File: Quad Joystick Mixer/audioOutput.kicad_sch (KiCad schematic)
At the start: 26 parts, among them J2 NMJ6HCD, U4 OPA1692xD

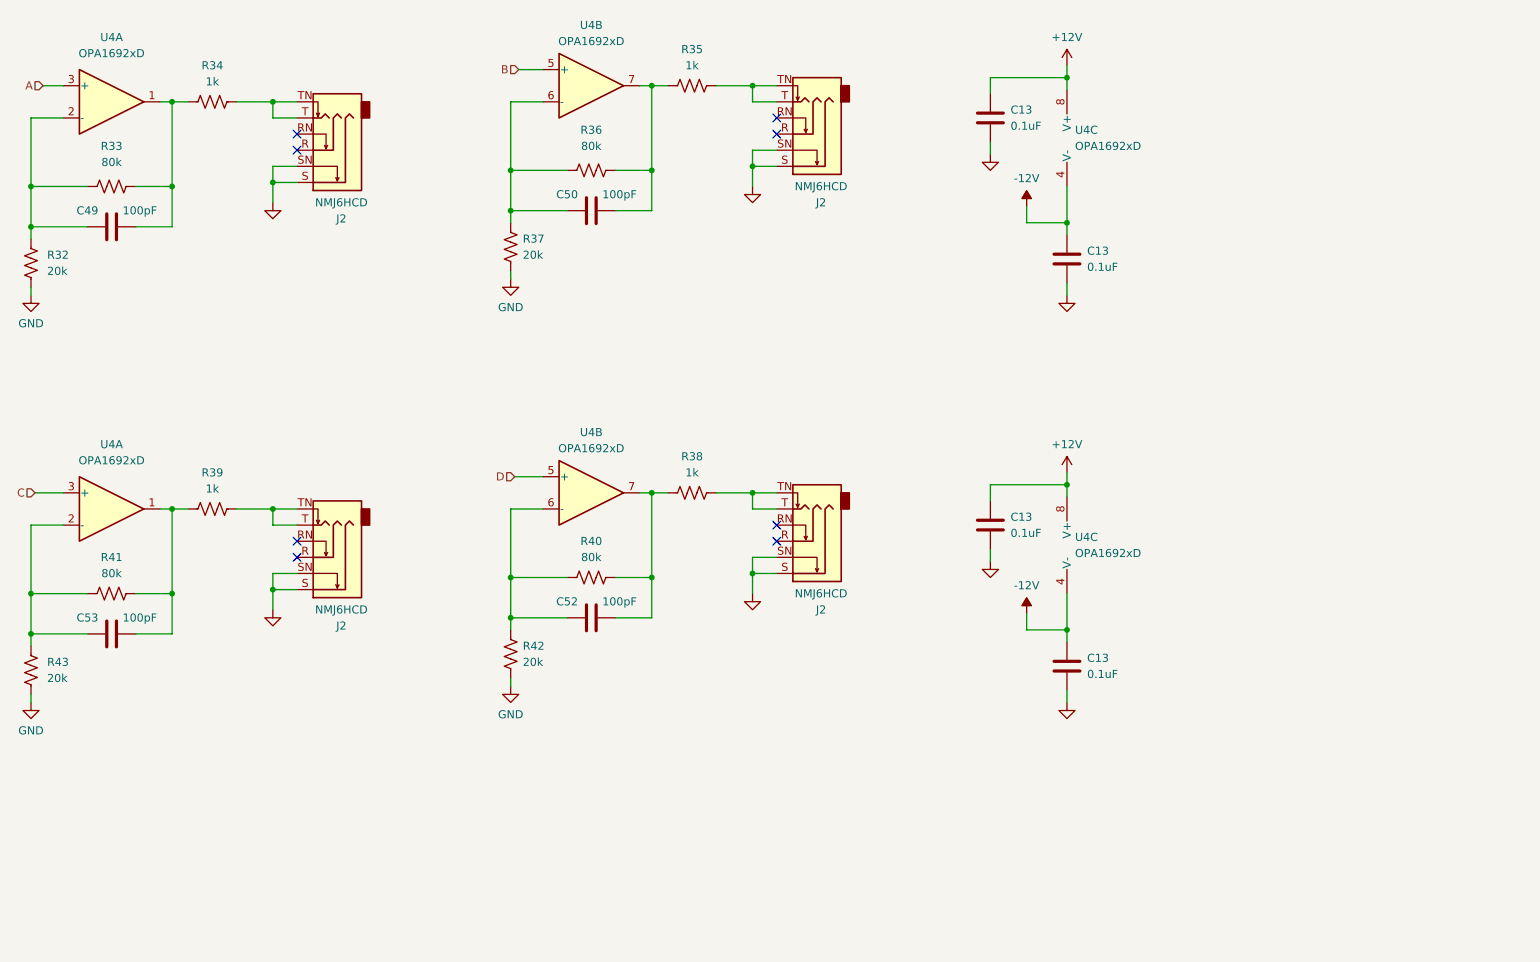
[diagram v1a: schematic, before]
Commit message: add in rotary circuit and some docs
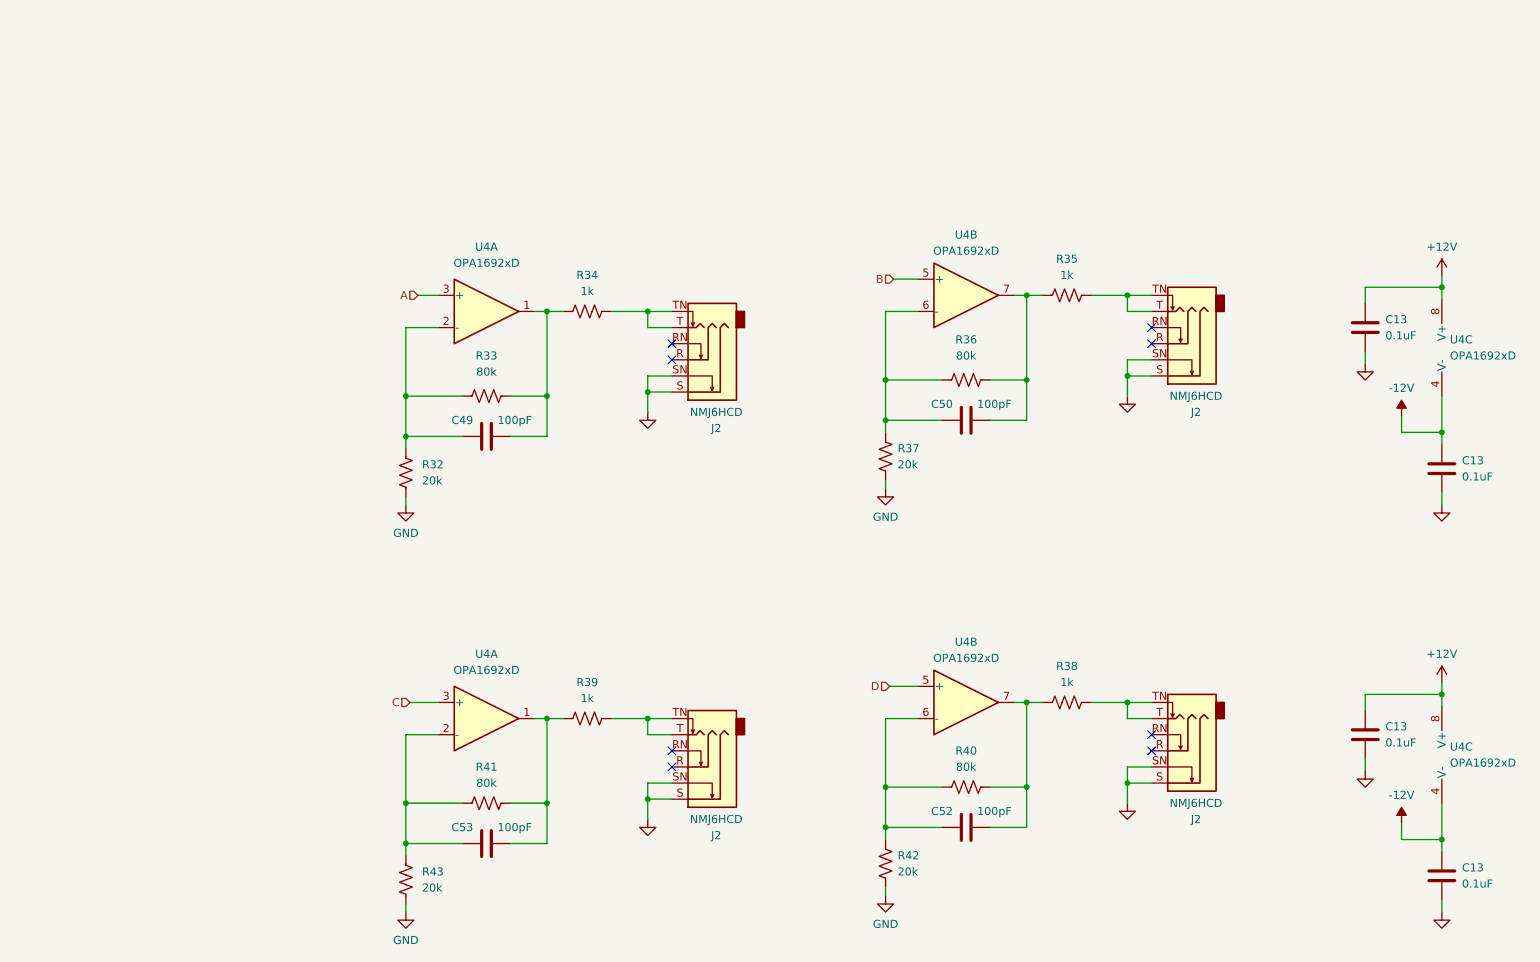
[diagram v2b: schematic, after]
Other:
- moved on the sheet: C13, C49, C50, C52, C53, J2, R32, R33, R34, R35, R36, R37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

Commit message: finished first draft of the schematic
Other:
- note added: "Audio Outputs"
- title: (none) -> Quadrophonic Joystick Mixer
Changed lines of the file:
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@@
   (paper "B")
   (title_block
+    (title "Quadrophonic Joystick Mixer")
     (date "2024-02-14")
+    (rev "P1")
   )
   (junction (at 224.155 147.32) (diameter 0) (color 0 0 0 0)
@@
     (stroke (width 0) (type default))
   )
+  (text "Audio Outputs" (at 157.48 45.085 0)
+    (effects (font (size 3.81 3.81) (thickness 0.508) bold) (justify left bottom))
+  )
   (hierarchical_label "D" (shape input) (at 202.565 144.78 180) (fields_autoplaced)

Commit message: ok the draft wasn't done but now i think it is
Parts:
- added TP1 (x4): TestPoint, TestPoint:TestPoint_THTPad_D1.5mm_Drill0.7mm, symbol Connector:TestPoint
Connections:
- net at J2.T, J2.TN, R39.1: now also TP1.1
- net at J2.T, J2.TN, R38.1: now also TP1.1
- net at J2.T, J2.TN, R34.1: now also TP1.1
- net at J2.T, J2.TN, R35.1: now also TP1.1
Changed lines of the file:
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@@
     (rev "P1")
   )
+  (junction (at 161.29 149.86) (diameter 0) (color 0 0 0 0)
+  )
+  (junction (at 161.29 85.725) (diameter 0) (color 0 0 0 0)
+  )
   (junction (at 224.155 147.32) (diameter 0) (color 0 0 0 0)
   )
@@
   (junction (at 201.93 160.655) (diameter 0) (color 0 0 0 0)
   )
+  (junction (at 236.855 147.32) (diameter 0) (color 0 0 0 0)
+  )
   (junction (at 240.03 95.885) (diameter 0) (color 0 0 0 0)
   )
@@
   )
   (junction (at 240.03 147.32) (diameter 0) (color 0 0 0 0)
+  )
+  (junction (at 236.855 83.185) (diameter 0) (color 0 0 0 0)
   )
   (junction (at 164.465 149.86) (diameter 0) (color 0 0 0 0)
@@
     (stroke (width 0) (type default))
   )
+  (wire (pts (xy 236.855 77.47) (xy 236.855 83.185))
+    (stroke (width 0) (type default))
+  )
   (wire (pts (xy 148.59 105.41) (xy 142.875 105.41))
     (stroke (width 0) (type default))
   )
+  (wire (pts (xy 236.855 83.185) (xy 240.03 83.185))
+    (stroke (width 0) (type default))
+  )
   (wire (pts (xy 243.84 149.86) (xy 240.03 149.86))
     (stroke (width 0) (type default))
@@
     (stroke (width 0) (type default))
   )
-  (wire (pts (xy 158.75 85.725) (xy 164.465 85.725))
+  (wire (pts (xy 158.75 85.725) (xy 161.29 85.725))
+    (stroke (width 0) (type default))
+  )
+  (wire (pts (xy 161.29 80.645) (xy 161.29 85.725))
     (stroke (width 0) (type default))
   )
@@
     (stroke (width 0) (type default))
   )
+  (wire (pts (xy 161.29 144.145) (xy 161.29 149.86))
+    (stroke (width 0) (type default))
+  )
   (wire (pts (xy 126.365 179.07) (xy 126.365 180.34))
     (stroke (width 0) (type default))
@@
     (stroke (width 0) (type default))
   )
+  (wire (pts (xy 236.855 147.32) (xy 240.03 147.32))
+    (stroke (width 0) (type default))
+  )
   (wire (pts (xy 146.685 85.725) (xy 148.59 85.725))
     (stroke (width 0) (type default))
@@
     (stroke (width 0) (type default))
   )
-  (wire (pts (xy 234.315 147.32) (xy 240.03 147.32))
+  (wire (pts (xy 234.315 147.32) (xy 236.855 147.32))
     (stroke (width 0) (type default))
   )
@@
     (stroke (width 0) (type default))
   )
-  (wire (pts (xy 158.75 149.86) (xy 164.465 149.86))
+  (wire (pts (xy 158.75 149.86) (xy 161.29 149.86))
     (stroke (width 0) (type default))
   )
@@
     (stroke (width 0) (type default))
   )
+  (wire (pts (xy 240.03 142.24) (xy 236.855 142.24))
+    (stroke (width 0) (type default))
+  )
   (wire (pts (xy 168.275 152.4) (xy 164.465 152.4))
     (stroke (width 0) (type default))
@@
     (stroke (width 0) (type default))
   )
+  (wire (pts (xy 238.76 77.47) (xy 236.855 77.47))
+    (stroke (width 0) (type default))
+  )
   (wire (pts (xy 207.01 85.725) (xy 201.93 85.725))
     (stroke (width 0) (type default))
   )
+  (wire (pts (xy 163.83 144.145) (xy 161.29 144.145))
+    (stroke (width 0) (type default))
+  )
   (wire (pts (xy 224.155 167.005) (xy 224.155 160.655))
     (stroke (width 0) (type default))
@@
     (stroke (width 0) (type default))
   )
-  (wire (pts (xy 234.315 83.185) (xy 240.03 83.185))
+  (wire (pts (xy 234.315 83.185) (xy 236.855 83.185))
     (stroke (width 0) (type default))
   )
@@
     (stroke (width 0) (type default))
   )
+  (wire (pts (xy 162.56 80.645) (xy 161.29 80.645))
+    (stroke (width 0) (type default))
+  )
   (wire (pts (xy 146.685 149.86) (xy 148.59 149.86))
     (stroke (width 0) (type default))
@@
     (stroke (width 0) (type default))
   )
+  (wire (pts (xy 161.29 149.86) (xy 164.465 149.86))
+    (stroke (width 0) (type default))
+  )
   (wire (pts (xy 127 147.32) (xy 131.445 147.32))
     (stroke (width 0) (type default))
@@
     (stroke (width 0) (type default))
   )
+  (wire (pts (xy 236.855 142.24) (xy 236.855 147.32))
+    (stroke (width 0) (type default))
+  )
   (wire (pts (xy 243.84 93.345) (xy 240.03 93.345))
     (stroke (width 0) (type default))
   )
   (wire (pts (xy 222.25 83.185) (xy 224.155 83.185))
+    (stroke (width 0) (type default))
+  )
+  (wire (pts (xy 161.29 85.725) (xy 164.465 85.725))
     (stroke (width 0) (type default))
   )
@@
     )
   )
+  (symbol (lib_id "Connector:TestPoint") (at 240.03 142.24 270) (unit 1)
+    (in_bom yes) (on_board yes) (dnp no) (fields_autoplaced)
+    (property "Reference" "TP1" (at 245.745 142.24 90)
+      (effects (font (size 1.27 1.27)) (justify left))
+    )
+    (property "Value" "TestPoint" (at 242.062 144.145 0)
+      (effects (font (size 1.27 1.27)) (justify left) hide)
+    )
+    (property "Footprint" "TestPoint:TestPoint_THTPad_D1.5mm_Drill0.7mm" (at 240.03 147.32 0)
+      (effects (font (size 1.27 1.27)) hide)
+    )
+    (property "Datasheet" "~" (at 240.03 147.32 0)
+      (effects (font (size 1.27 1.27)) hide)
+    )
+    (pin "1")
+    (instances
+      (project "Quad Joystick Mixer"
+        (path "/e9da4955-68c1-4335-ab8e-8a9cc0328d2d/70e873e8-c2f7-42de-91d7-3f147d0d972e"
+          (reference "TP1") (unit 1)
+        )
+        (path "/e9da4955-68c1-4335-ab8e-8a9cc0328d2d/df381643-9329-42d2-97be-3d7265bc1cca"
+          (reference "TP19") (unit 1)
+        )
+      )
+    )
+  )
   (symbol (lib_id "power:GND") (at 126.365 180.34 0) (unit 1)
     (in_bom yes) (on_board yes) (dnp no) (fields_autoplaced)
@@
         (path "/e9da4955-68c1-4335-ab8e-8a9cc0328d2d/df381643-9329-42d2-97be-3d7265bc1cca"
           (reference "C54") (unit 1)
+        )
+      )
+    )
+  )
+  (symbol (lib_id "Connector:TestPoint") (at 162.56 80.645 270) (unit 1)
+    (in_bom yes) (on_board yes) (dnp no) (fields_autoplaced)
+    (property "Reference" "TP1" (at 168.275 80.645 90)
+      (effects (font (size 1.27 1.27)) (justify left))
+    )
+    (property "Value" "TestPoint" (at 164.592 82.55 0)
+      (effects (font (size 1.27 1.27)) (justify left) hide)
+    )
+    (property "Footprint" "TestPoint:TestPoint_THTPad_D1.5mm_Drill0.7mm" (at 162.56 85.725 0)
+      (effects (font (size 1.27 1.27)) hide)
+    )
+    (property "Datasheet" "~" (at 162.56 85.725 0)
+      (effects (font (size 1.27 1.27)) hide)
+    )
+    (pin "1")
+    (instances
+      (project "Quad Joystick Mixer"
+        (path "/e9da4955-68c1-4335-ab8e-8a9cc0328d2d/70e873e8-c2f7-42de-91d7-3f147d0d972e"
+          (reference "TP1") (unit 1)
+        )
+        (path "/e9da4955-68c1-4335-ab8e-8a9cc0328d2d/df381643-9329-42d2-97be-3d7265bc1cca"
+          (reference "TP16") (unit 1)
         )
       )
@@
     )
   )
+  (symbol (lib_id "Connector:TestPoint") (at 238.76 77.47 270) (unit 1)
+    (in_bom yes) (on_board yes) (dnp no) (fields_autoplaced)
+    (property "Reference" "TP1" (at 244.475 77.47 90)
+      (effects (font (size 1.27 1.27)) (justify left))
+    )
+    (property "Value" "TestPoint" (at 240.792 79.375 0)
+      (effects (font (size 1.27 1.27)) (justify left) hide)
+    )
+    (property "Footprint" "TestPoint:TestPoint_THTPad_D1.5mm_Drill0.7mm" (at 238.76 82.55 0)
+      (effects (font (size 1.27 1.27)) hide)
+    )
+    (property "Datasheet" "~" (at 238.76 82.55 0)
+      (effects (font (size 1.27 1.27)) hide)
+    )
+    (pin "1")
+    (instances
+      (project "Quad Joystick Mixer"
+        (path "/e9da4955-68c1-4335-ab8e-8a9cc0328d2d/70e873e8-c2f7-42de-91d7-3f147d0d972e"
+          (reference "TP1") (unit 1)
+        )
+        (path "/e9da4955-68c1-4335-ab8e-8a9cc0328d2d/df381643-9329-42d2-97be-3d7265bc1cca"
+          (reference "TP17") (unit 1)
+        )
+      )
+    )
+  )
   (symbol (lib_id "power:+12V") (at 289.56 80.01 0) (unit 1)
     (in_bom yes) (on_board yes) (dnp no) (fields_autoplaced)
@@
         )
       )
+    )
+  )
+  (symbol (lib_id "Connector:TestPoint") (at 163.83 144.145 270) (unit 1)
+    (in_bom yes) (on_board yes) (dnp no) (fields_autoplaced)
+    (property "Reference" "TP1" (at 169.545 144.145 90)
+      (effects (font (size 1.27 1.27)) (justify left))
+    )
+    (property "Value" "TestPoint" (at 165.862 146.05 0)
+      (effects (font (size 1.27 1.27)) (justify left) hide)
+    )
+    (property "Footprint" "TestPoint:TestPoint_THTPad_D1.5mm_Drill0.7mm" (at 163.83 149.225 0)
+      (effects (font (size 1.27 1.27)) hide)
+    )
+    (property "Datasheet" "~" (at 163.83 149.225 0)
+      (effects (font (size 1.27 1.27)) hide)
+    )
+    (pin "1")
+    (instances
+      (project "Quad Joystick Mixer"
+        (path "/e9da4955-68c1-4335-ab8e-8a9cc0328d2d/70e873e8-c2f7-42de-91d7-3f147d0d972e"
+          (reference "TP1") (unit 1)
+        )
+        (path "/e9da4955-68c1-4335-ab8e-8a9cc0328d2d/df381643-9329-42d2-97be-3d7265bc1cca"
+          (reference "TP18") (unit 1)
+        )
+      )

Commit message: clean up after review, working through BOM
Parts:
- removed C13 (x2): 0.1uF, Capacitor_SMD:C_0805_2012Metric_Pad1.18x1.45mm_HandSolder, symbol Device:C
- removed C53: 100pF, symbol Device:C
- removed J2 (x2): NMJ6HCD, Eyewool Connectors:NMJ6HCD, symbol Connector_Audio:AudioJack3_Switch
- removed R40, R41: 80k, symbol Device:R_US
- removed R42, R43: 20k, symbol Device:R_US
- removed TP1 (x2): TestPoint, TestPoint:TestPoint_THTPad_D1.5mm_Drill0.7mm, symbol Connector:TestPoint
- added C13 (x2): 0.1uF, Capacitor_SMD:C_0805_2012Metric_Pad1.18x1.45mm_HandSolder, symbol Device:C
- added C51: 330pF, Capacitor_SMD:C_0805_2012Metric_Pad1.18x1.45mm_HandSolder, symbol Device:C
- added J2 (x2): NMJ6HCD, Eyewool Connectors:NMJ6HCD, symbol Connector_Audio:AudioJack3_Switch
- added TP1 (x2): TestPoint, TestPoint:TestPoint_THTPad_D1.5mm_Drill0.7mm, symbol Connector:TestPoint
- C49, C50, C52: value 100pF -> 330pF; footprint (none) -> Capacitor_SMD:C_0805_2012Metric_Pad1.18x1.45mm_HandSolder; DK PN (none) -> 399-C0805C331J5GAC7800CT-ND; MPN (none) -> C0805C331J5GAC7800
- R33, R36: value 80k -> 20k
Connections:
- net +12V: now also C13.1
- net -12V: now also C13.1
- net A: now also C49.1, R33.2, U4.2 (-); no longer U4.3 (+)
- net B: now also C50.1, R32.2, U4.6 (-); no longer U4.5 (+)
- net C: now also C52.1, R37.2, U4.2 (-); no longer U4.3 (+)
- net D: now also R36.2, U4.6 (-), C51.1; no longer U4.5 (+)
- net GND: now also U4.3 (+), U4.3 (+), U4.5 (+), U4.5 (+), C13.2, C13.2, J2.S, J2.S, J2.SN, J2.SN; no longer R32.2, R37.2
- net at R38.1: now also J2.T, J2.TN, TP1.1
- net at R39.1: now also J2.T, J2.TN, TP1.1
- net at R39.2, U4.1: now also C52.2, R37.1
- net at R38.2, U4.7: now also R36.1, C51.2; no longer C52.2
- net at C50.2, R35.2, U4.7: now also R32.1; no longer R36.1
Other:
- note added: "Each input to mix node has 10k series"
- moved on the sheet: C49, R33
